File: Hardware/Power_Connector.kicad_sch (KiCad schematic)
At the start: 3 parts, among them J4 AMASS XT60 Male, J5 AMASS XT60 Female

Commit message: removed holes from bom
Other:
- company: (none) -> MiniModucard System
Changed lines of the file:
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@@
 	(title_block
 		(title "MMS3 Hat template small (Change Me)")
-		(date "2026-02-25")
+		(date "2077-13-75")
 		(rev "A")
-		(comment 1 "Made by Wojciech Szafrański")
+		(company "MiniModucard System")
+		(comment 1 "Wojciech Szafrański")
 		(comment 2 "Designed in poland")
 	)

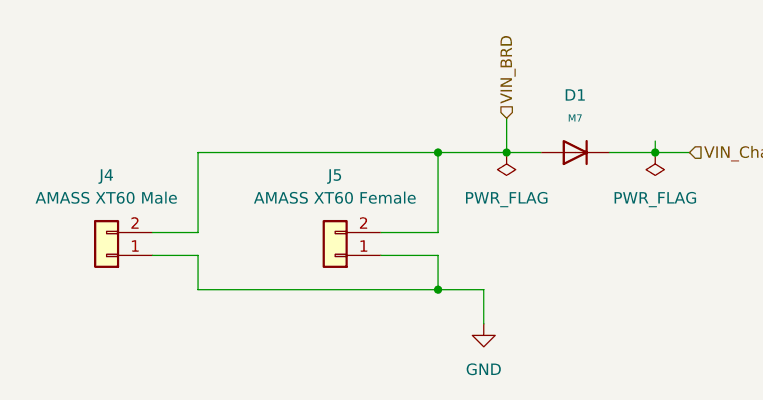
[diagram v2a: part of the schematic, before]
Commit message: changed numbering to per-sheet
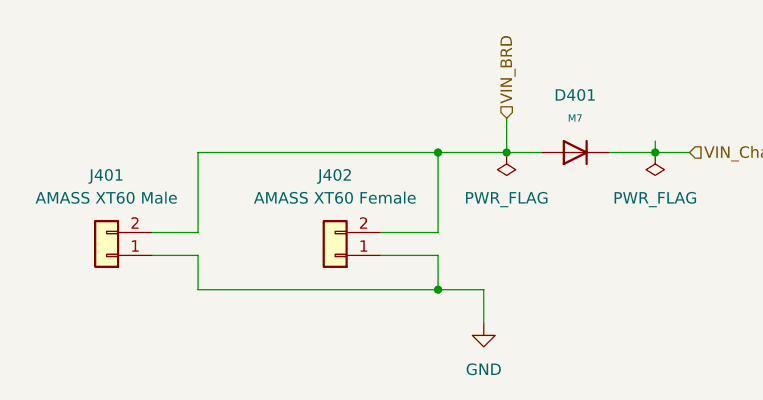
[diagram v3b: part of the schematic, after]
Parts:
- renumbered D1 to D401, J4 to J401, J5 to J402
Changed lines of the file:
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@@
 		(dnp no)
 		(fields_autoplaced yes)
-		(property "Reference" "J4"
+		(property "Reference" "J401"
 			(at 115.57 88.9 0)
 			(show_name no)
@@
 			(project "MMS3_hat_templates"
 				(path "/6596548a-44e0-46d8-8624-fd71cf4a3e17/f11c3b61-ae6a-4858-9d37-bbf426f44fb0"
-					(reference "J4")
+					(reference "J401")
 					(unit 1)
 				)
@@
 		(dnp no)
 		(fields_autoplaced yes)
-		(property "Reference" "J5"
+		(property "Reference" "J402"
 			(at 140.97 88.9 0)
 			(show_name no)
@@
 			(project "MMS3_hat_templates"
 				(path "/6596548a-44e0-46d8-8624-fd71cf4a3e17/f11c3b61-ae6a-4858-9d37-bbf426f44fb0"
-					(reference "J5")
+					(reference "J402")
 					(unit 1)
 				)
@@
 		(dnp no)
 		(fields_autoplaced yes)
-		(property "Reference" "#FLG02"
+		(property "Reference" "#FLG0402"
 			(at 176.53 88.265 0)
 			(hide yes)
@@
 			(project "MMS3_hat_templates"
 				(path "/6596548a-44e0-46d8-8624-fd71cf4a3e17/f11c3b61-ae6a-4858-9d37-bbf426f44fb0"
-					(reference "#FLG02")
+					(reference "#FLG0402")
 					(unit 1)
 				)
@@
 		(dnp no)
 		(fields_autoplaced yes)
-		(property "Reference" "D1"
+		(property "Reference" "D401"
 			(at 167.64 80.01 90)
 			(show_name no)
@@
 			(project "MMS3_hat_templates"
 				(path "/6596548a-44e0-46d8-8624-fd71cf4a3e17/f11c3b61-ae6a-4858-9d37-bbf426f44fb0"
-					(reference "D1")
+					(reference "D401")
 					(unit 1)
 				)
@@
 		(dnp no)
 		(fields_autoplaced yes)
-		(property "Reference" "#FLG03"
+		(property "Reference" "#FLG0401"
 			(at 160.02 88.265 0)
 			(hide yes)
@@
 			(project "MMS3_hat_templates"
 				(path "/6596548a-44e0-46d8-8624-fd71cf4a3e17/f11c3b61-ae6a-4858-9d37-bbf426f44fb0"
-					(reference "#FLG03")
+					(reference "#FLG0401")
 					(unit 1)
 				)
@@
 		(dnp no)
 		(fields_autoplaced yes)
-		(property "Reference" "#PWR040"
+		(property "Reference" "#PWR0401"
 			(at 157.48 111.76 0)
 			(hide yes)
@@
 			(project "MMS3_hat_templates"
 				(path "/6596548a-44e0-46d8-8624-fd71cf4a3e17/f11c3b61-ae6a-4858-9d37-bbf426f44fb0"
-					(reference "#PWR040")
+					(reference "#PWR0401")
 					(unit 1)
 				)

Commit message: major rework of template
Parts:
- removed J401: AMASS XT60 Male, XT60:AMASS_XT60PW-M_1x02_P7.20mm_Horizontal, symbol Connector_Generic:Conn_01x02
- removed J402: AMASS XT60 Female, XT60:AMASS_XT60PW-F_1x02_P7.20mm_Horizontal, symbol Connector_Generic:Conn_01x02
- added CN401: XT60PW-M, lcsc_footprints:C98732_CONN-TH_XT60PW-M, symbol lcsc_imported:XT60PW-M
- added U401: XT60PW-F_C428722, lcsc_footprints:C428722_TH_2P-XT60PW-F, symbol lcsc_imported:XT60PW-F_C428722
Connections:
- net GND: now also CN401.1 (-), U401.4 (-)
- net VIN_BRD: now also CN401.2 (+), U401.3 (+)
- no-connect marks 0 -> 4

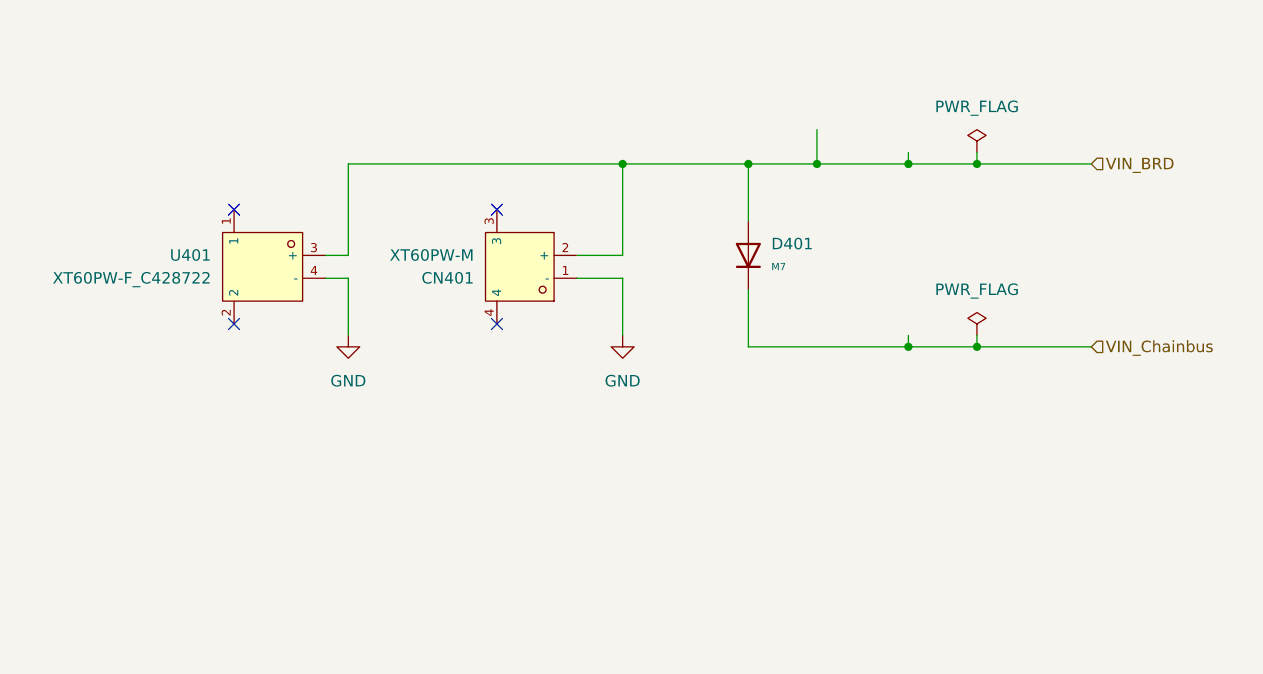
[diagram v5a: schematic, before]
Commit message: removed I2C connector, added VIN led
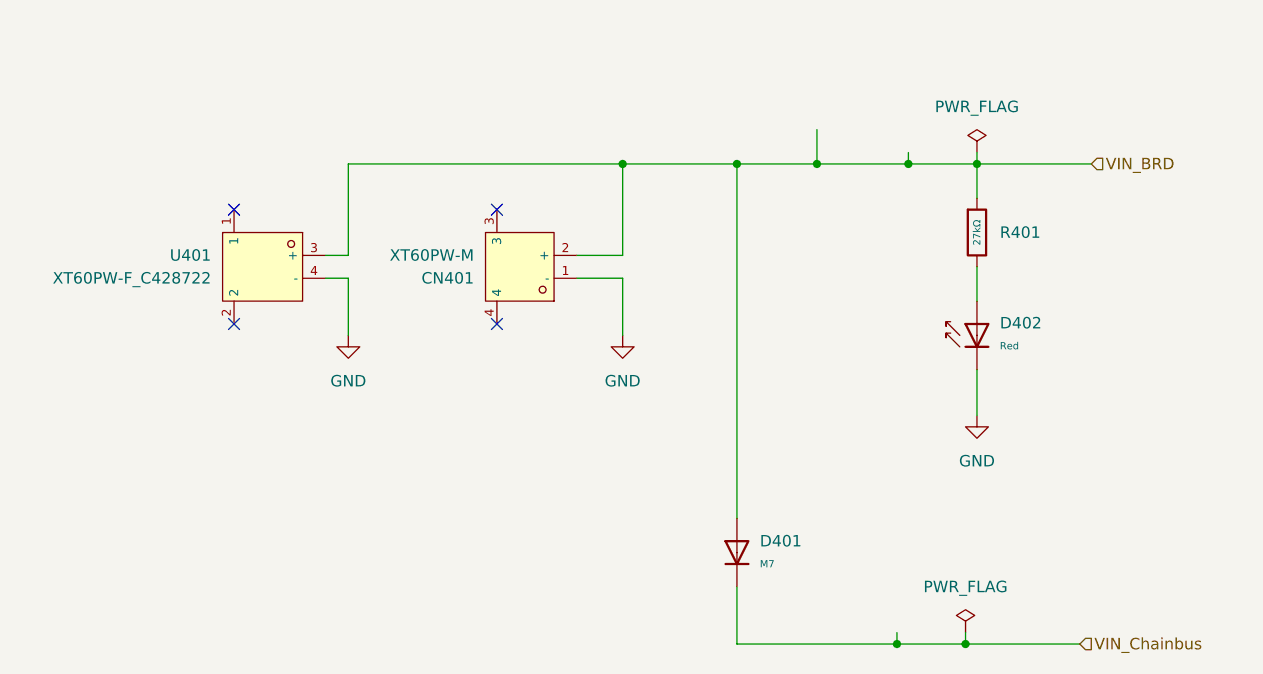
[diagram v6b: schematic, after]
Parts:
- added D402: Red, PCM_JLCPCB:D_0603, symbol PCM_JLCPCB-Diodes:LED,0603,Red
- added R401: 27kΩ, PCM_JLCPCB:R_0603, symbol PCM_JLCPCB-Resistors:0603,27kΩ
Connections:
- net GND: now also D402.1
- net VIN_BRD: now also R401.1
- new net: D402.2, R401.2
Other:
- moved on the sheet: D401
